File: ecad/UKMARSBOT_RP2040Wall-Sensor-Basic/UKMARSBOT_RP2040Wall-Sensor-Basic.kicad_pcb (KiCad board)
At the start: 2 copper layers, 80 x 31.2 mm, 27 parts, among them J1 Conn_01x16, T1 BC33716, T2 BC33716

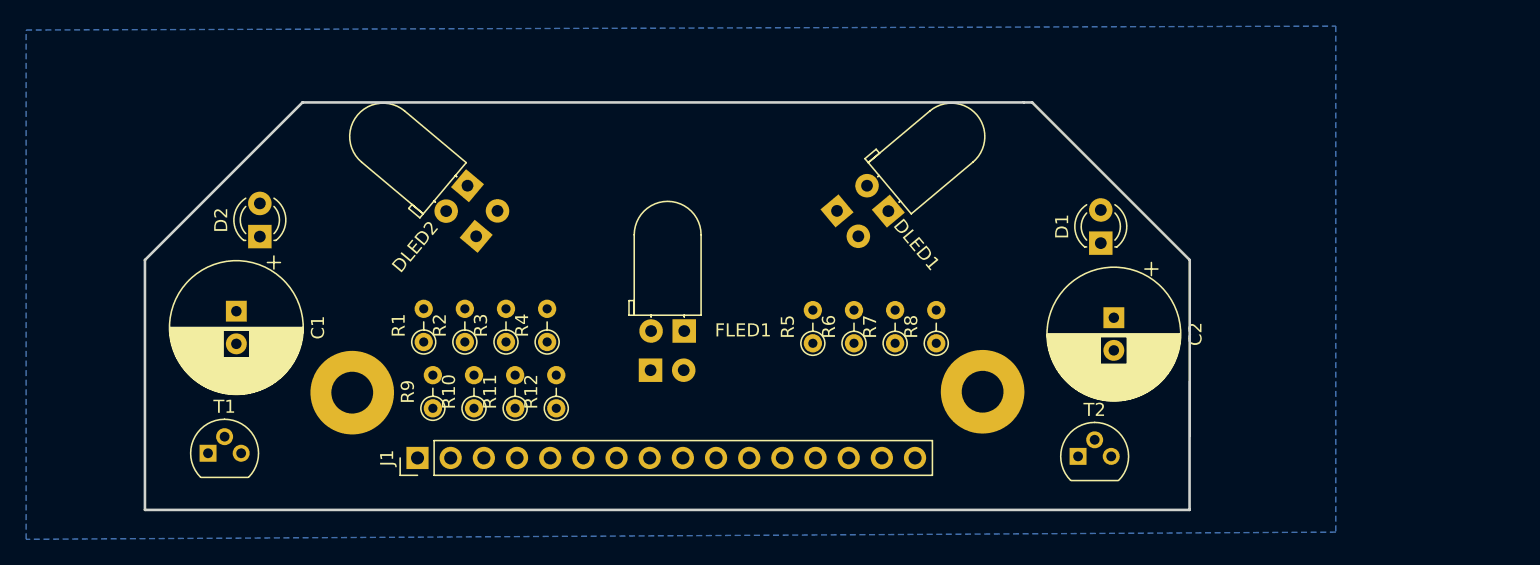
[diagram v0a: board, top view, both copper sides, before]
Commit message: Update to 5v rail and layouts across all 3 boards
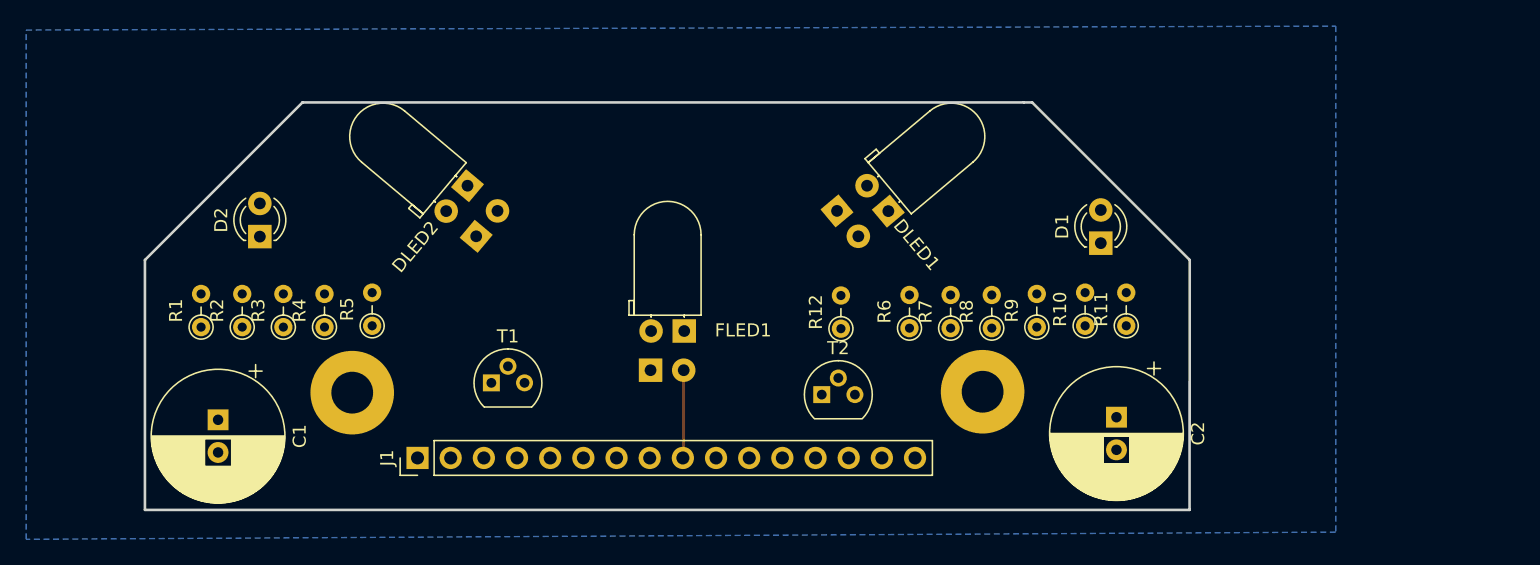
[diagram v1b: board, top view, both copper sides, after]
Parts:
- moved R11 47.2 mm to (175.2, 139.8)
- moved R10 47.2 mm to (172.0, 139.8)
- moved R9 46.7 mm to (168.3, 139.9)
- moved R5 33.8 mm to (117.4, 139.8)
- moved R12 22.6 mm to (153.3, 140.0)
- moved T1 22.4 mm to (126.5, 144.2)
- moved T2 20.2 mm to (151.8, 145.1)
- moved R3 17.1 mm to (110.6, 139.9)
- moved R4 17.1 mm to (113.8, 139.9)
- moved R1 17.1 mm to (104.3, 139.9)
- moved R2 17.1 mm to (107.5, 139.9)
- moved C1 8.43 mm to (105.6, 147.0)
- moved C2 7.62 mm to (174.4, 146.8)
- moved R6 4.41 mm to (158.6, 140.0)
- moved R7 4.41 mm to (161.7, 140.0)
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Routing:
- net SEN0AIP: track 0.00 -> 6.75 mm
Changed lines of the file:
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@@
 	(footprint "Package_TO_SOT_THT:TO-92"
 		(layer "F.Cu")
-		(at 104.83 149.56)
+		(at 126.53 144.17)
 		(descr "TO-92 leads molded, narrow, drill 0.75mm (see NXP sot054_po.pdf)")
 		(tags "to-92 sc-43 sc-43a sot54 PA33 transistor")
@@
 	(footprint "Capacitor_THT:CP_Radial_D10.0mm_P2.50mm"
 		(layer "F.Cu")
-		(at 174.2 139.1823 -90)
+		(at 174.4 146.8 -90)
 		(descr "CP, Radial series, Radial, pin pitch=2.50mm, , diameter=10mm, Electrolytic Capacitor")
 		(tags "CP Radial series Radial pin pitch 2.50mm  diameter 10mm Electrolytic Capacitor")
@@
 	(footprint "Resistor_THT:R_Axial_DIN0204_L3.6mm_D1.6mm_P2.54mm_Vertical"
 		(layer "F.Cu")
-		(at 157.45 141.14 90)
+		(at 161.7 139.98 90)
 		(descr "Resistor, Axial_DIN0204 series, Axial, Vertical, pin pitch=2.54mm, 0.167W, length*diameter=3.6*1.6mm^2, http://cdn-reichelt.de/documents/datenblatt/B400/1_4W%23YAG.pdf")
 		(tags "Resistor Axial_DIN0204 series Axial Vertical pin pitch 2.54mm 0.167W length 3.6mm diameter 1.6mm")
@@
 	(footprint "Capacitor_THT:CP_Radial_D10.0mm_P2.50mm"
 		(layer "F.Cu")
-		(at 107 138.6823 -90)
+		(at 105.6 147 -90)
 		(descr "CP, Radial series, Radial, pin pitch=2.50mm, , diameter=10mm, Electrolytic Capacitor")
 		(tags "CP Radial series Radial pin pitch 2.50mm  diameter 10mm Electrolytic Capacitor")
@@
 	(footprint "Resistor_THT:R_Axial_DIN0204_L3.6mm_D1.6mm_P2.54mm_Vertical"
 		(layer "F.Cu")
-		(at 128.35 146.12 90)
+		(at 175.15 139.8 90)
 		(descr "Resistor, Axial_DIN0204 series, Axial, Vertical, pin pitch=2.54mm, 0.167W, length*diameter=3.6*1.6mm^2, http://cdn-reichelt.de/documents/datenblatt/B400/1_4W%23YAG.pdf")
 		(tags "Resistor Axial_DIN0204 series Axial Vertical pin pitch 2.54mm 0.167W length 3.6mm diameter 1.6mm")
@@
 	(footprint "Package_TO_SOT_THT:TO-92"
 		(layer "F.Cu")
-		(at 171.46 149.8)
+		(at 151.83 145.07)
 		(descr "TO-92 leads molded, narrow, drill 0.75mm (see NXP sot054_po.pdf)")
 		(tags "to-92 sc-43 sc-43a sot54 PA33 transistor")
@@
 	(footprint "Resistor_THT:R_Axial_DIN0204_L3.6mm_D1.6mm_P2.54mm_Vertical"
 		(layer "F.Cu")
-		(at 160.6 141.14 90)
+		(at 164.85 139.98 90)
 		(descr "Resistor, Axial_DIN0204 series, Axial, Vertical, pin pitch=2.54mm, 0.167W, length*diameter=3.6*1.6mm^2, http://cdn-reichelt.de/documents/datenblatt/B400/1_4W%23YAG.pdf")
 		(tags "Resistor Axial_DIN0204 series Axial Vertical pin pitch 2.54mm 0.167W length 3.6mm diameter 1.6mm")
@@
 	(footprint "Resistor_THT:R_Axial_DIN0204_L3.6mm_D1.6mm_P2.54mm_Vertical"
 		(layer "F.Cu")
-		(at 151.15 141.14 90)
+		(at 117.4 139.8 90)
 		(descr "Resistor, Axial_DIN0204 series, Axial, Vertical, pin pitch=2.54mm, 0.167W, length*diameter=3.6*1.6mm^2, http://cdn-reichelt.de/documents/datenblatt/B400/1_4W%23YAG.pdf")
 		(tags "Resistor Axial_DIN0204 series Axial Vertical pin pitch 2.54mm 0.167W length 3.6mm diameter 1.6mm")
@@
 	(footprint "Resistor_THT:R_Axial_DIN0204_L3.6mm_D1.6mm_P2.54mm_Vertical"
 		(layer "F.Cu")
-		(at 127.65 141.04 90)
+		(at 110.6 139.9 90)
 		(descr "Resistor, Axial_DIN0204 series, Axial, Vertical, pin pitch=2.54mm, 0.167W, length*diameter=3.6*1.6mm^2, http://cdn-reichelt.de/documents/datenblatt/B400/1_4W%23YAG.pdf")
 		(tags "Resistor Axial_DIN0204 series Axial Vertical pin pitch 2.54mm 0.167W length 3.6mm diameter 1.6mm")
@@
 	(footprint "Resistor_THT:R_Axial_DIN0204_L3.6mm_D1.6mm_P2.54mm_Vertical"
 		(layer "F.Cu")
-		(at 131.5 146.12 90)
+		(at 153.3 140.02 90)
 		(descr "Resistor, Axial_DIN0204 series, Axial, Vertical, pin pitch=2.54mm, 0.167W, length*diameter=3.6*1.6mm^2, http://cdn-reichelt.de/documents/datenblatt/B400/1_4W%23YAG.pdf")
 		(tags "Resistor Axial_DIN0204 series Axial Vertical pin pitch 2.54mm 0.167W length 3.6mm diameter 1.6mm")
@@
 	(footprint "Resistor_THT:R_Axial_DIN0204_L3.6mm_D1.6mm_P2.54mm_Vertical"
 		(layer "F.Cu")
-		(at 121.35 141.04 90)
+		(at 104.3 139.9 90)
 		(descr "Resistor, Axial_DIN0204 series, Axial, Vertical, pin pitch=2.54mm, 0.167W, length*diameter=3.6*1.6mm^2, http://cdn-reichelt.de/documents/datenblatt/B400/1_4W%23YAG.pdf")
 		(tags "Resistor Axial_DIN0204 series Axial Vertical pin pitch 2.54mm 0.167W length 3.6mm diameter 1.6mm")
@@
 	(footprint "Resistor_THT:R_Axial_DIN0204_L3.6mm_D1.6mm_P2.54mm_Vertical"
 		(layer "F.Cu")
-		(at 124.5 141.04 90)
+		(at 107.45 139.9 90)
 		(descr "Resistor, Axial_DIN0204 series, Axial, Vertical, pin pitch=2.54mm, 0.167W, length*diameter=3.6*1.6mm^2, http://cdn-reichelt.de/documents/datenblatt/B400/1_4W%23YAG.pdf")
 		(tags "Resistor Axial_DIN0204 series Axial Vertical pin pitch 2.54mm 0.167W length 3.6mm diameter 1.6mm")
@@
 	(footprint "Resistor_THT:R_Axial_DIN0204_L3.6mm_D1.6mm_P2.54mm_Vertical"
 		(layer "F.Cu")
-		(at 122.05 146.12 90)
+		(at 168.3 139.9 90)
 		(descr "Resistor, Axial_DIN0204 series, Axial, Vertical, pin pitch=2.54mm, 0.167W, length*diameter=3.6*1.6mm^2, http://cdn-reichelt.de/documents/datenblatt/B400/1_4W%23YAG.pdf")
 		(tags "Resistor Axial_DIN0204 series Axial Vertical pin pitch 2.54mm 0.167W length 3.6mm diameter 1.6mm")
@@
 	(footprint "Resistor_THT:R_Axial_DIN0204_L3.6mm_D1.6mm_P2.54mm_Vertical"
 		(layer "F.Cu")
-		(at 130.8 141.04 90)
+		(at 113.75 139.9 90)
 		(descr "Resistor, Axial_DIN0204 series, Axial, Vertical, pin pitch=2.54mm, 0.167W, length*diameter=3.6*1.6mm^2, http://cdn-reichelt.de/documents/datenblatt/B400/1_4W%23YAG.pdf")
 		(tags "Resistor Axial_DIN0204 series Axial Vertical pin pitch 2.54mm 0.167W length 3.6mm diameter 1.6mm")
@@
 	(footprint "Resistor_THT:R_Axial_DIN0204_L3.6mm_D1.6mm_P2.54mm_Vertical"
 		(layer "F.Cu")
-		(at 154.3 141.14 90)
+		(at 158.55 139.98 90)
 		(descr "Resistor, Axial_DIN0204 series, Axial, Vertical, pin pitch=2.54mm, 0.167W, length*diameter=3.6*1.6mm^2, http://cdn-reichelt.de/documents/datenblatt/B400/1_4W%23YAG.pdf")
 		(tags "Resistor Axial_DIN0204 series Axial Vertical pin pitch 2.54mm 0.167W length 3.6mm diameter 1.6mm")
@@
 	(footprint "Resistor_THT:R_Axial_DIN0204_L3.6mm_D1.6mm_P2.54mm_Vertical"
 		(layer "F.Cu")
-		(at 125.2 146.12 90)
+		(at 172 139.8 90)
 		(descr "Resistor, Axial_DIN0204 series, Axial, Vertical, pin pitch=2.54mm, 0.167W, length*diameter=3.6*1.6mm^2, http://cdn-reichelt.de/documents/datenblatt/B400/1_4W%23YAG.pdf")
 		(tags "Resistor Axial_DIN0204 series Axial Vertical pin pitch 2.54mm 0.167W length 3.6mm diameter 1.6mm")
@@
 		(fp_arc
 			(start -1.289998 -7.370004)
-			(mid 1.270007 -9.929988)
+			(mid 1.270007 -9.929987)
 			(end 3.830007 -7.369998)
 			(stroke
@@
 		)
 	)
+	(segment
+		(start 141.26 143.2)
+		(end 141.26 149.855)
+		(width 0.2)
+		(layer "F.Cu")
+		(net 9)
+	)
+	(segment
+		(start 141.26 149.855)
+		(end 141.195 149.92)
+		(width 0.2)
+		(layer "F.Cu")
+		(net 9)
+	)
 	(zone

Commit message: Flush mount resistors and diodes
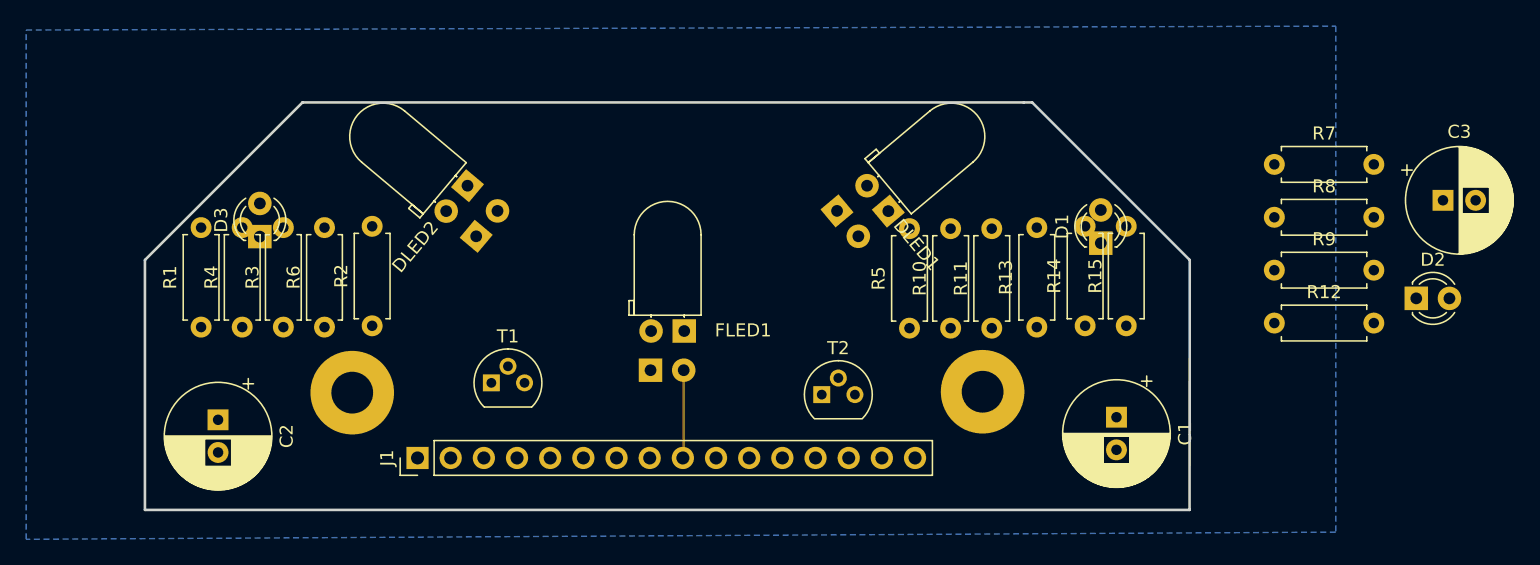
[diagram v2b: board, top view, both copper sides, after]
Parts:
- added C3: 330uF, 16v, Capacitor_THT:CP_Radial_D8.0mm_P2.50mm, F.Cu at (199.4, 130.2)
- added D2: LED, LED_THT:LED_D3.0mm, F.Cu at (197.4, 137.7)
- added R7: 33R, Resistor_THT:R_Axial_DIN0207_L6.3mm_D2.5mm_P7.62mm_Horizontal, F.Cu at (186.5, 127.4)
- added R8: 33R, Resistor_THT:R_Axial_DIN0207_L6.3mm_D2.5mm_P7.62mm_Horizontal, F.Cu at (186.5, 131.5)
- added R9: 33R, Resistor_THT:R_Axial_DIN0207_L6.3mm_D2.5mm_P7.62mm_Horizontal, F.Cu at (186.5, 135.5)
- C1: renamed from C2; value 10uF -> 100uF, 16v; footprint Capacitor_THT:CP_Radial_D10.0mm_P2.50mm -> Capacitor_THT:CP_Radial_D8.0mm_P2.50mm
- C2: renamed from C1; value 10uF -> 100uF, 16v; footprint Capacitor_THT:CP_Radial_D10.0mm_P2.50mm -> Capacitor_THT:CP_Radial_D8.0mm_P2.50mm
- R1, R3: footprint Resistor_THT:R_Axial_DIN0204_L3.6mm_D1.6mm_P2.54mm_Vertical -> Resistor_THT:R_Axial_DIN0207_L6.3mm_D2.5mm_P7.62mm_Horizontal
- R10: renamed from R7; footprint Resistor_THT:R_Axial_DIN0204_L3.6mm_D1.6mm_P2.54mm_Vertical -> Resistor_THT:R_Axial_DIN0207_L6.3mm_D2.5mm_P7.62mm_Horizontal
- R11: renamed from R8; value R -> 2k2; footprint Resistor_THT:R_Axial_DIN0204_L3.6mm_D1.6mm_P2.54mm_Vertical -> Resistor_THT:R_Axial_DIN0207_L6.3mm_D2.5mm_P7.62mm_Horizontal
- R12: value 220R -> 1K0; footprint Resistor_THT:R_Axial_DIN0204_L3.6mm_D1.6mm_P2.54mm_Vertical -> Resistor_THT:R_Axial_DIN0207_L6.3mm_D2.5mm_P7.62mm_Horizontal
- R13: renamed from R9; value R -> 2k2; footprint Resistor_THT:R_Axial_DIN0204_L3.6mm_D1.6mm_P2.54mm_Vertical -> Resistor_THT:R_Axial_DIN0207_L6.3mm_D2.5mm_P7.62mm_Horizontal
- R14: renamed from R10; footprint Resistor_THT:R_Axial_DIN0204_L3.6mm_D1.6mm_P2.54mm_Vertical -> Resistor_THT:R_Axial_DIN0207_L6.3mm_D2.5mm_P7.62mm_Horizontal
- R15: renamed from R11; value R -> 2k2; footprint Resistor_THT:R_Axial_DIN0204_L3.6mm_D1.6mm_P2.54mm_Vertical -> Resistor_THT:R_Axial_DIN0207_L6.3mm_D2.5mm_P7.62mm_Horizontal
- R2: renamed from R5; footprint Resistor_THT:R_Axial_DIN0204_L3.6mm_D1.6mm_P2.54mm_Vertical -> Resistor_THT:R_Axial_DIN0207_L6.3mm_D2.5mm_P7.62mm_Horizontal
- R4: renamed from R2; footprint Resistor_THT:R_Axial_DIN0204_L3.6mm_D1.6mm_P2.54mm_Vertical -> Resistor_THT:R_Axial_DIN0207_L6.3mm_D2.5mm_P7.62mm_Horizontal
- R5: renamed from R6; footprint Resistor_THT:R_Axial_DIN0204_L3.6mm_D1.6mm_P2.54mm_Vertical -> Resistor_THT:R_Axial_DIN0207_L6.3mm_D2.5mm_P7.62mm_Horizontal
- R6: renamed from R4; footprint Resistor_THT:R_Axial_DIN0204_L3.6mm_D1.6mm_P2.54mm_Vertical -> Resistor_THT:R_Axial_DIN0207_L6.3mm_D2.5mm_P7.62mm_Horizontal
- moved R12 33.2 mm to (186.5, 139.6), turned to 0 degrees
- renumbered D2 to D3
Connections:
- C1 pad 1: Net-(FLED1-A) -> Net-(C1-Pad1)
- C2 pad 1: Net-(DLED1-A) -> Net-(C2-Pad1)
- DLED2 pad 1: Net-(DLED2-K) -> Net-(DLED1-K)
- DLED2 pad 2: Net-(DLED1-K) -> Net-(DLED2-A)
- FPD1 pad 1: Net-(FPD1-C) -> Vcc
- LDPD1 pad 1: Net-(FPD1-C) -> Vcc
- R10 pad 1: SEN3DI0 -> SEN4DI0
- R12 pad 1: Net-(FPD1-C) -> SEN3DI0
- R12 pad 2: Vcc -> Net-(D2-A)
- R14 pad 1: SEN4DI0 -> SEN2DI0
- R2 pad 2: Net-(DLED1-A) -> Net-(C2-Pad1)
- R5 pad 2: Net-(FLED1-A) -> Net-(C1-Pad1)
- RDPD1 pad 1: Net-(FPD1-C) -> Vcc
- T1 pad 3: Net-(DLED2-K) -> Net-(DLED1-K)

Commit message: Updates components based on issues #27 and  #28 Placement and routing of PCB has been done
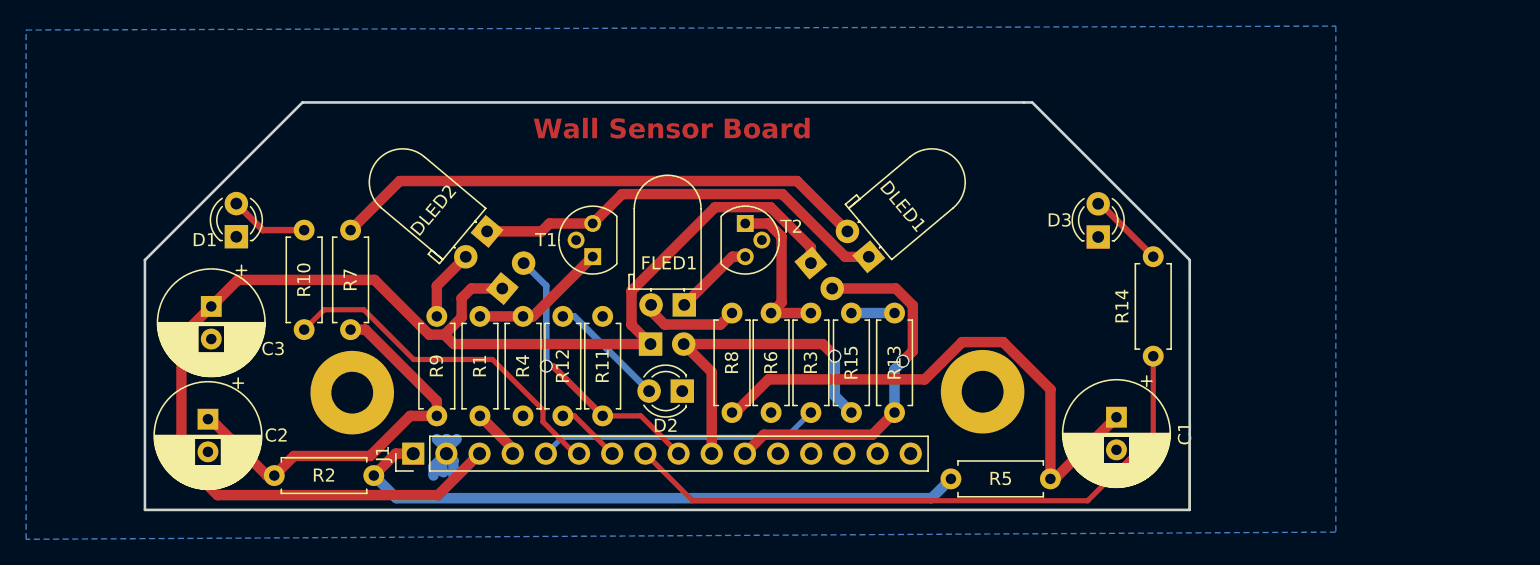
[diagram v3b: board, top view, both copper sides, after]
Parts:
- R4, R6: value 10K -> 47K
- T1, T2: value BC33716 -> BC337-40
- moved C3 94.7 mm to (105.1, 138.3), turned to -90 degrees
- moved R7 71.9 mm to (115.7, 140.1), turned to 90 degrees
- moved D1 66.2 mm to (107.0, 133.0)
- moved R9 65.1 mm to (122.4, 146.7), turned to 90 degrees
- moved D3 64.2 mm to (173.0, 133.0)
- moved D2 56.7 mm to (141.1, 144.8), turned to 180 degrees
- moved R12 54.9 mm to (132.0, 146.7), turned to 90 degrees
- moved R10 49.5 mm to (112.2, 140.1)
- moved R8 42.2 mm to (145.0, 138.8), turned to -90 degrees
- moved R3 40.9 mm to (151.0, 146.4)
- moved R6 34.2 mm to (148.0, 138.8), turned to -90 degrees
- moved R11 30.5 mm to (135.1, 146.7)
- moved R1 22.4 mm to (125.7, 146.7)
- moved R15 22.1 mm to (154.1, 146.4)
- moved R4 21.5 mm to (129.0, 139.1), turned to -90 degrees
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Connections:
- FPD1 pad 2: SEN0AIP -> SEN1AIP
- LDPD1 pad 2: SEN1AIP -> SEN0AIP
- R1 pad 1: SEN1DI0 -> SEN0DI0
- R10 pad 1: SEN4DI0 -> SEN2DI0
- R11 pad 1: SEN1AIP -> SEN0AIP
- R14 pad 1: SEN2DI0 -> SEN4DI0
- R15 pad 1: SEN0AIP -> SEN1AIP
- R3 pad 1: SEN0DI0 -> SEN1DI0
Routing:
- net Vcc: track 0.00 -> 105.0 mm
- net 5V: track 0.00 -> 49.2 mm
- net SEN4DI0: track 0.00 -> 48.5 mm
- net Net-(C1-Pad1): track 0.00 -> 42.0 mm
- net Net-(DLED1-A): track 0.00 -> 41.2 mm
- net Net-(DLED1-K): track 0.00 -> 32.4 mm
- net Net-(C2-Pad1): track 0.00 -> 31.2 mm
- net SEN2AIP: track 0.00 -> 28.3 mm, vias 0 -> 1
- net SEN2DI0: track 0.00 -> 26.8 mm
- net SEN1AIP: track 0.00 -> 26.1 mm, vias 0 -> 1
- net SEN1DI0: track 0.00 -> 21.6 mm
- net SEN0AIP: track 6.75 -> 21.5 mm, vias 0 -> 1
- net Net-(T2-B): track 0.00 -> 12.4 mm
- net GND: track 0.00 -> 12.2 mm
- net Net-(T1-B): track 0.00 -> 10.5 mm
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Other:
- board text added: "${designer}"
- board text added: "Wall Sensor Board"
- board text removed: "Designed by ${designer}"
